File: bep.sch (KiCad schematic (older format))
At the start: 28 parts

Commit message: first version of schematic finished
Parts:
- removed D?: D, symbol Device:D
- removed JP?: Jumper, symbol Device:Jumper
- added C1: 100n, Capacitor_SMD:C_1206_3216Metric_Pad1.42x1.75mm_HandSolder, symbol Device:C
- added C?: 10u, symbol Device:CP
- added D4: D, symbol Device:D
- added D? (x4): LED, symbol Device:LED
- added J2: Conn_01x24, symbol Connector_Generic:Conn_01x24
- added Q1, Q2, Q3, Q4, Q5, Q6: SMBTA42, Package_TO_SOT_SMD:SOT-23, symbol Device:Q_NPN_BEC
- added R1, R2, R3: 100k, symbol Device:R
- added R10, R20, R4, R6, R7, R8, R9: 10k, symbol Device:R
- added R11, R12: 47 2W, symbol Device:R
- added R?: 100, symbol Device:R
- added R? (x4): 350, symbol Device:R
- added U1: HCF4028B, Package_SO:SOIC-16_3.9x9.9mm_P1.27mm, symbol 4xxx:4028
- added U2: LM1117-5.0, symbol Regulator_Linear:LM1117-5.0
- R16: renamed from R?; value 10k -> 100k
- gave numbers to parts that had none: 25
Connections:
- net labels added: 12V_IGN, GEAR1, GEAR2, GEAR3, GEAR4, GEAR5, GEAR_NEUTRAL
- net labels removed: 12V
- wire segments 96 -> 184
- no-connect marks 1 -> 5
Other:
- note added: "Decode gear signals"
- note added: "Provide excitation current for alternator"
- note added: "RMP signal"
- note removed: "INSERT 5V LDO here"
- note removed: "K100 Lunchbox Adapter"
- moved on the sheet: C2, D2, D3, J1, Q7, R13, R14, R15, R16, R17, R18, R19

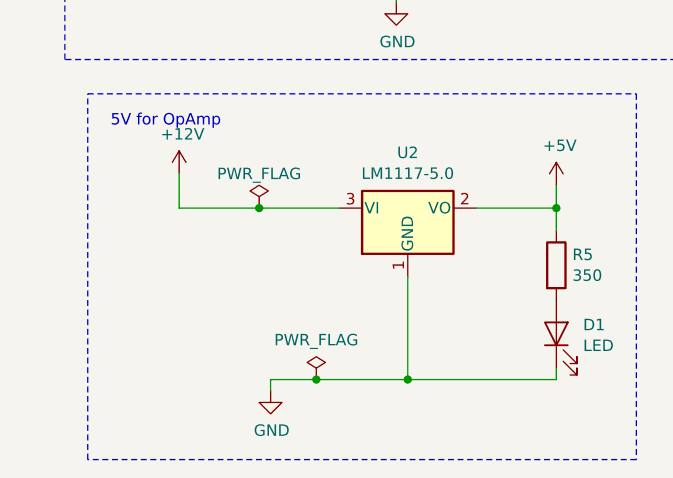
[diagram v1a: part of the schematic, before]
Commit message: add TSV diode to library
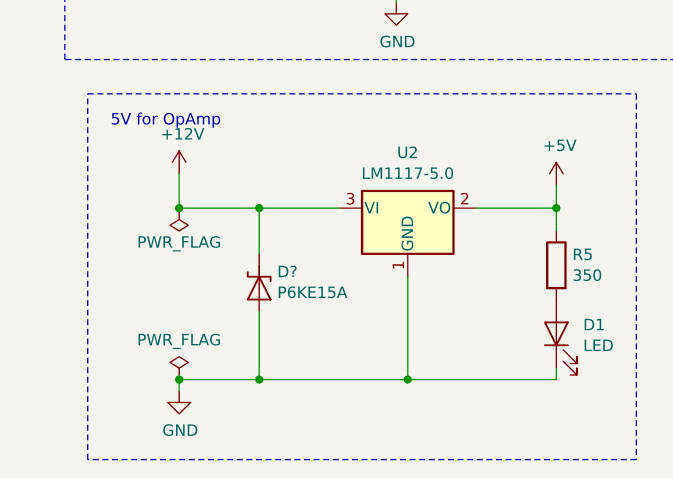
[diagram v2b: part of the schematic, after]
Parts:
- added D?: P6KE15A, Diode_THT:D_DO-15_P12.70mm_Horizontal, symbol bep:D_TVS_uni
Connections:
- wire segments 184 -> 186
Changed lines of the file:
@@
 $EndComp
 Wire Wire Line
-	1450 7350 1450 7300
-Wire Wire Line
-	1450 7300 1650 7300
-Connection ~ 1650 7300
+	1050 7350 1050 7300
+Connection ~ 1050 7300
 $Comp
 L power:PWR_FLAG #FLG0102
 U 1 1 5CCB4D9A
-P 1650 7300
-F 0 "#FLG0102" H 1650 7375 50  0001 C CNN
-F 1 "PWR_FLAG" H 1650 7473 50  0000 C CNN
-F 2 "" H 1650 7300 50  0001 C CNN
-F 3 "~" H 1650 7300 50  0001 C CNN
-	1    1650 7300
-	1    0    0    -1
-$EndComp
-Wire Wire Line
-	1400 6550 1750 6550
+P 1050 7300
+F 0 "#FLG0102" H 1050 7375 50  0001 C CNN
+F 1 "PWR_FLAG" H 1050 7473 50  0000 C CNN
+F 2 "" H 1050 7300 50  0001 C CNN
+F 3 "~" H 1050 7300 50  0001 C CNN
+	1    1050 7300
+	1    0    0    -1
+$EndComp
 Wire Wire Line
 	1050 6550 1400 6550
-Connection ~ 1400 6550
+Connection ~ 1050 6550
 $Comp
 L power:PWR_FLAG #FLG0101
 U 1 1 5CCB4539
-P 1400 6550
-F 0 "#FLG0101" H 1400 6625 50  0001 C CNN
-F 1 "PWR_FLAG" H 1400 6700 50  0000 C CNN
-F 2 "" H 1400 6550 50  0001 C CNN
-F 3 "~" H 1400 6550 50  0001 C CNN
-	1    1400 6550
-	1    0    0    -1
+P 1050 6550
+F 0 "#FLG0101" H 1050 6625 50  0001 C CNN
+F 1 "PWR_FLAG" H 1050 6700 50  0000 C CNN
+F 2 "" H 1050 6550 50  0001 C CNN
+F 3 "~" H 1050 6550 50  0001 C CNN
+	1    1050 6550
+	1    0    0    1
 $EndComp
 $Comp
@@
 L power:GND #PWR0101
 U 1 1 5CCB1309
-P 1450 7350
-F 0 "#PWR0101" H 1450 7100 50  0001 C CNN
-F 1 "GND" H 1455 7177 50  0000 C CNN
-F 2 "" H 1450 7350 50  0001 C CNN
-F 3 "" H 1450 7350 50  0001 C CNN
-	1    1450 7350
-	1    0    0    -1
-$EndComp
-Wire Wire Line
-	1650 7300 2050 7300
+P 1050 7350
+F 0 "#PWR0101" H 1050 7100 50  0001 C CNN
+F 1 "GND" H 1055 7177 50  0000 C CNN
+F 2 "" H 1050 7350 50  0001 C CNN
+F 3 "" H 1050 7350 50  0001 C CNN
+	1    1050 7350
+	1    0    0    -1
+$EndComp
+Wire Wire Line
+	1050 7300 1400 7300
 Wire Wire Line
 	2050 6850 2050 7300
@@
 Wire Notes Line
 	3500 6000 3500 7650
+$Comp
+L bep:D_TVS_uni D?
+U 1 1 5D24CD62
+P 1400 6850
+F 0 "D?" V 1379 6929 50  0000 L CNN
+F 1 "P6KE15A" V 1470 6929 50  0000 L CNN
+F 2 "Diode_THT:D_DO-15_P12.70mm_Horizontal" H 1400 6850 50  0001 C CNN
+F 3 "~" H 1400 6850 50  0001 C CNN
+	1    1400 6850
+	0    1    1    0
+$EndComp
+Wire Wire Line
+	1400 6750 1400 6550
+Connection ~ 1400 6550
+Wire Wire Line
+	1400 6550 1750 6550
+Wire Wire Line
+	1400 7000 1400 7300
+Connection ~ 1400 7300
+Wire Wire Line
+	1400 7300 2050 7300
 $EndSCHEMATC

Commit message: finished logic of schematic
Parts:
- removed C?: 10u, symbol Device:CP
- removed R?: 100, symbol Device:R
- removed U3: LTC2054, Package_TO_SOT_SMD:TSOT-23-5_HandSoldering, symbol bep:LTC2054
- added C? (x2): 10u, symbol Device:CP
- added C?: 220n, symbol Device:C
- added C?: 56n, symbol Device:C
- added C? (x2): 100n, symbol Device:C
- added D? (x2): D, symbol Device:D
- added JP?: Jumper_3_Bridged12, symbol Jumper:Jumper_3_Bridged12
- added Q? (x2): SMBTA42, Package_TO_SOT_SMD:SOT-23, symbol Device:Q_NPN_BEC
- added R?: 4.7k, symbol Device:R
- added R? (x2): 2.2k, symbol Device:R
- added R? (x5): 10k, symbol Device:R
- added R?: 1k, symbol Device:R
- added U? (x3): LM2904, symbol Amplifier_Operational:LM2904
- gave numbers to parts that had none: 9
- renumbered D9 to D10, D2 to D11, D3 to D12, D4 to D13, D10 to D14, D1 to D2, D6 to D7, D7 to D8, D8 to D9, JP2 to JP1, JP3 to JP2, JP4 to JP3, JP5 to JP4, R8 to R11, R9 to R13, R10 to R14, R11 to R15, R12 to R16, R13 to R17, R14 to R18, R15 to R19, R16 to R21, R17 to R22, R18 to R23, R19 to R24, R20 to R25
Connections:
- wire segments 186 -> 243
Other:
- note added: "Jumper position:\n1-2: 12V rect signal, pulse to GND\n2-3: filtered ignition coil signal"
- note added: "RPM Signal conditioning"
- note removed: "RMP signal"
- moved on the sheet: C2, D1, D11, D12, D13, D14, J1, J2, Q7, Q8, Q9, R15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

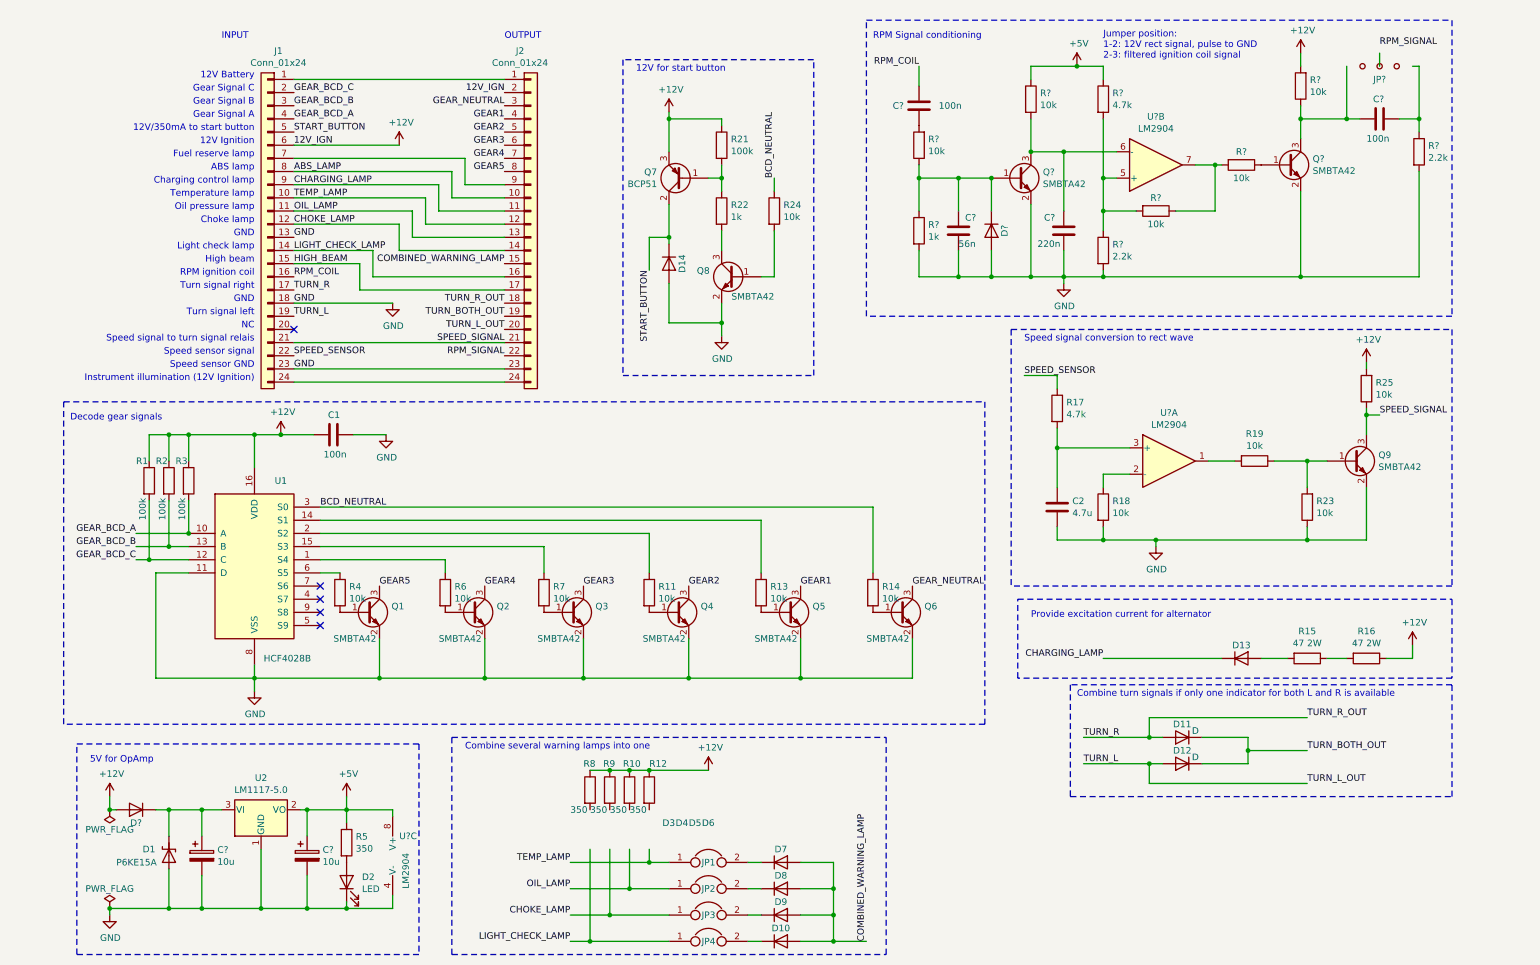
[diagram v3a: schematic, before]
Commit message: finalized schematic
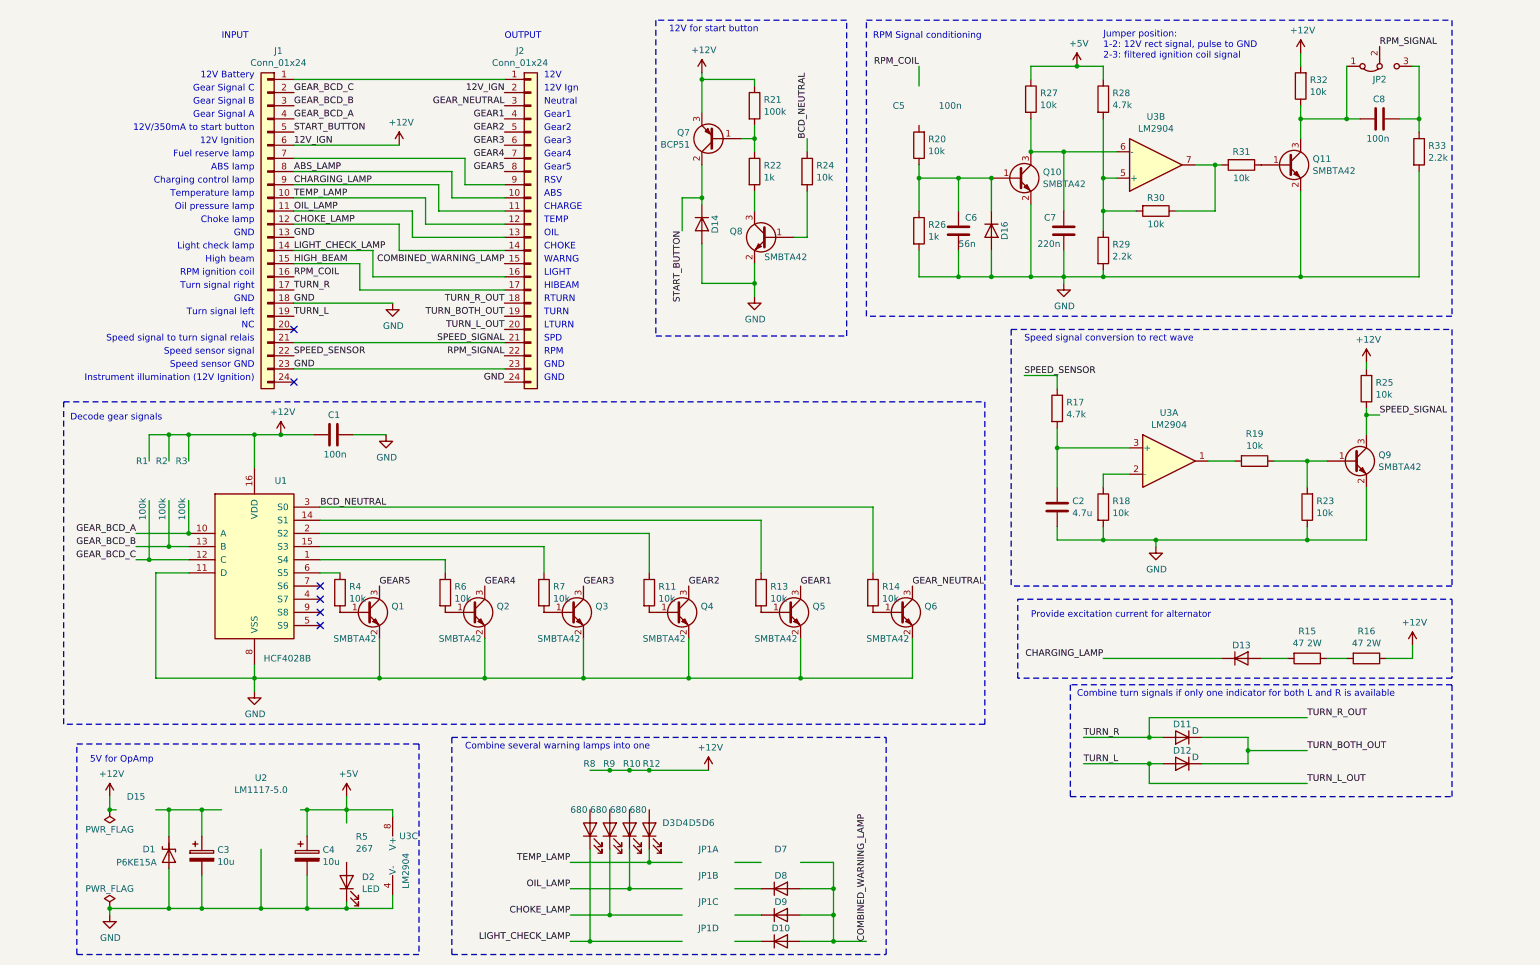
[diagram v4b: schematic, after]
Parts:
- removed JP1, JP2, JP3, JP4: Jumper, symbol Device:Jumper
- added JP1: Jumper_4x2, Connector_PinHeader_2.54mm:PinHeader_2x04_P2.54mm_Vertical, symbol bep:Jumper_4x2
- C2: footprint (none) -> Capacitor_SMD:C_1206_3216Metric_Pad1.42x1.75mm_HandSolder
- C3, C4: renamed from C?; footprint (none) -> Capacitor_SMD:CP_Elec_4x5.8
- C5: renamed from C?; footprint (none) -> Capacitor_THT:C_Rect_L18.0mm_W8.0mm_P15.00mm_FKS3_FKP3
- C6: renamed from C?; footprint (none) -> Capacitor_SMD:C_0603_1608Metric_Pad1.05x0.95mm_HandSolder
- C7, C8: renamed from C?; footprint (none) -> Capacitor_SMD:C_1206_3216Metric_Pad1.42x1.75mm_HandSolder
- D10, D11, D12, D13, D14, D7, D8, D9: footprint (none) -> Diode_SMD:D_SMA_Handsoldering
- D15, D16: renamed from D?; footprint (none) -> Diode_SMD:D_SMA_Handsoldering
- D2, D3, D4, D5, D6: footprint (none) -> LED_SMD:LED_1206_3216Metric_Pad1.42x1.75mm_HandSolder
- R1, R2, R21, R3: footprint (none) -> Resistor_SMD:R_1206_3216Metric_Pad1.42x1.75mm_HandSolder
- R10, R12, R8, R9: value 350 -> 680; footprint (none) -> Resistor_SMD:R_0805_2012Metric_Pad1.15x1.40mm_HandSolder
- R11, R13, R14, R17, R18, R19, R22, R23, R24, R25, R4, R6, R7: footprint (none) -> Resistor_SMD:R_0805_2012Metric_Pad1.15x1.40mm_HandSolder
- R15, R16: footprint (none) -> Resistor_THT:R_Axial_DIN0614_L14.3mm_D5.7mm_P25.40mm_Horizontal
- R20, R26, R27, R28, R29, R30, R31, R32, R33: renamed from R?; footprint (none) -> Resistor_SMD:R_0805_2012Metric_Pad1.15x1.40mm_HandSolder
- R5: value 350 -> 267; footprint (none) -> Resistor_SMD:R_1206_3216Metric_Pad1.42x1.75mm_HandSolder
- U2: footprint (none) -> Package_TO_SOT_SMD:SOT-223-3_TabPin2
- U3: renamed from U?; footprint (none) -> Package_SO:SO-8_3.9x4.9mm_P1.27mm
- gave numbers to parts that had none: 3
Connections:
- wire segments 243 -> 241
- no-connect marks 5 -> 6
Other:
- note added: "12V"
- note added: "12V Ign"
- note added: "ABS"
- note added: "CHARGE"
- note added: "CHOKE"
- note added: "Gear1"
- note added: "Gear2"
- note added: "Gear3"
- note added: "Gear4"
- note added: "Gear5"
- note added: "HIBEAM"
- note added: "LIGHT"
- note added: "LTURN"
- note added: "Neutral"
- note added: "OIL"
- note added: "RPM"
- note added: "RSV"
- note added: "RTURN"
- note added: "SPD"
- note added: "TEMP"
- note added: "TURN"
- note added: "WARNG"
- moved on the sheet: D14, Q7, Q8, R21, R22, R24

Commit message: output signals grouped to several connectors
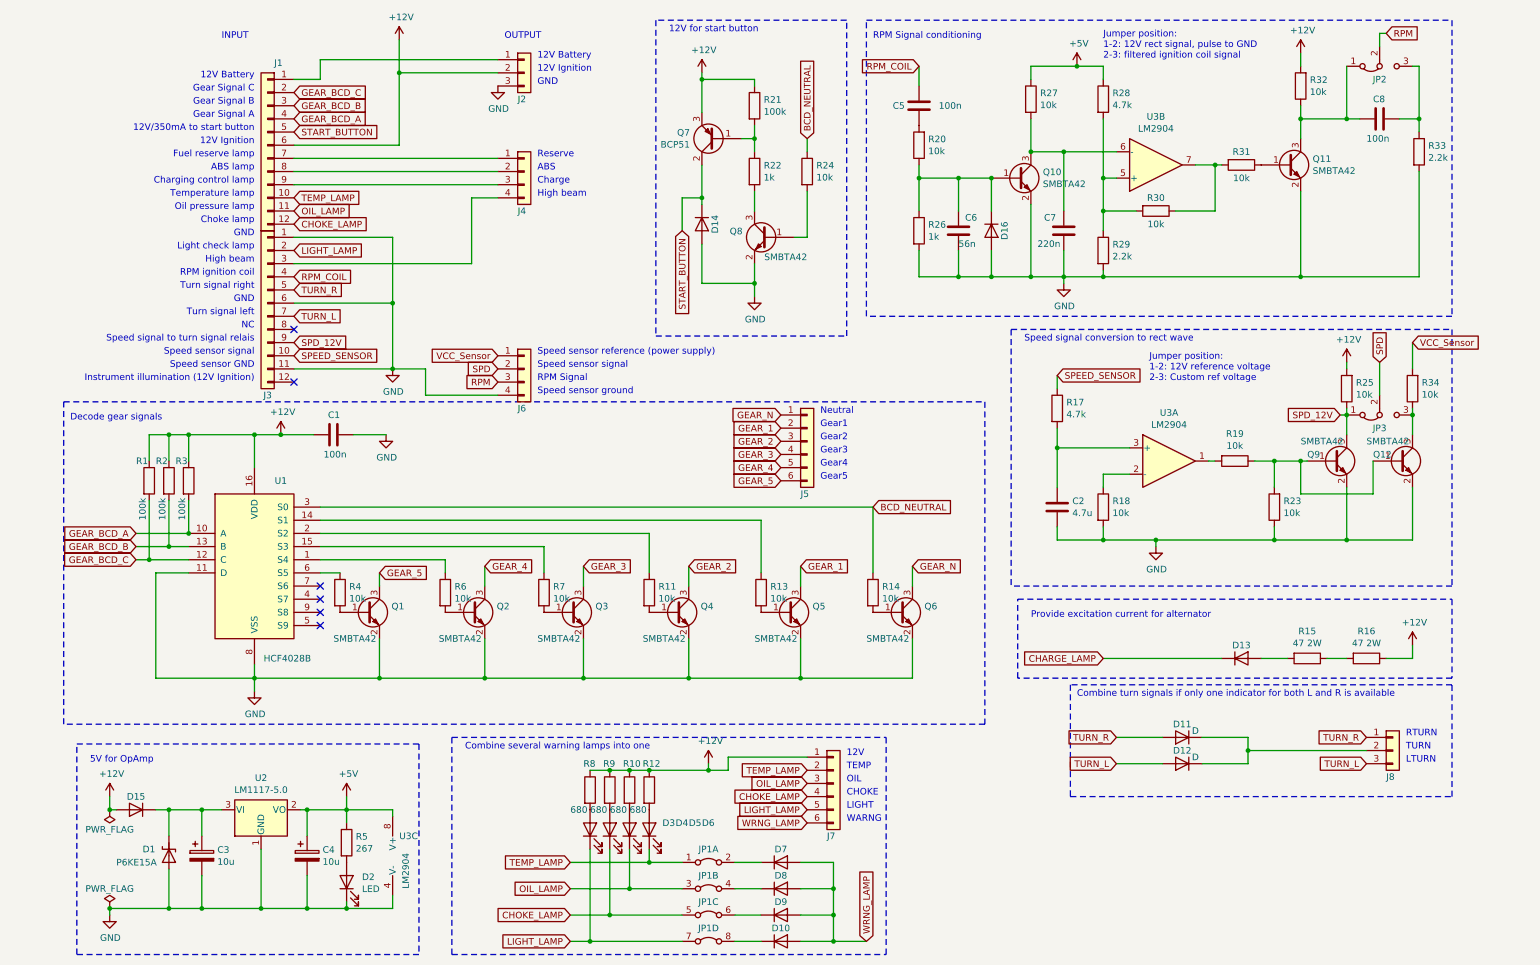
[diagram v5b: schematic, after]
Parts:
- removed J1, J2: Conn_01x24, symbol Connector_Generic:Conn_01x24
- added J1, J3: Conn_01x12, Connector_PinHeader_2.54mm:PinHeader_1x12_P2.54mm_Vertical, symbol Connector_Generic:Conn_01x12
- added J2, J8: Conn_01x03, Connector_PinHeader_2.54mm:PinHeader_1x03_P2.54mm_Vertical, symbol Connector_Generic:Conn_01x03
- added J4, J6: Conn_01x03, Connector_PinHeader_2.54mm:PinHeader_1x04_P2.54mm_Vertical, symbol Connector_Generic:Conn_01x04
- added J5, J7: Conn_01x06, Connector_PinHeader_2.54mm:PinHeader_1x06_P2.54mm_Vertical, symbol Connector_Generic:Conn_01x06
- added JP3: Jumper_3_Bridged12, Connector_PinHeader_2.54mm:PinHeader_1x03_P2.54mm_Vertical, symbol Jumper:Jumper_3_Bridged12
- added Q12: SMBTA42, Package_TO_SOT_SMD:SOT-23, symbol Device:Q_NPN_BEC
- added R34: 10k, Resistor_SMD:R_0805_2012Metric_Pad1.15x1.40mm_HandSolder, symbol Device:R
- D10, D11, D12, D13, D14, D15, D16, D7, D8, D9: footprint Diode_SMD:D_SMA_Handsoldering -> Diode_SMD:D_0603_1608Metric_Pad1.05x0.95mm_HandSolder
- JP2: footprint (none) -> Connector_PinHeader_2.54mm:PinHeader_1x03_P2.54mm_Vertical
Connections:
- net labels added: CHARGE_LAMP, GEAR_1, GEAR_2, GEAR_3, GEAR_4, GEAR_5, GEAR_N, LIGHT_LAMP, RPM, SPD, SPD_12V, VCC_Sensor, WRNG_LAMP
- net labels removed: 12V_IGN, ABS_LAMP, CHARGING_LAMP, COMBINED_WARNING_LAMP, GEAR1, GEAR2, GEAR3, GEAR4, GEAR5, GEAR_NEUTRAL, HIGH_BEAM, LIGHT_CHECK_LAMP, RPM_SIGNAL, SPEED_SIGNAL, TURN_BOTH_OUT, TURN_L_OUT, TURN_R_OUT
- wire segments 241 -> 248
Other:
- note added: "Charge"
- note added: "Jumper position:\n1-2: 12V reference voltage\n2-3: Custom ref voltage"
- note added: "RPM Signal"
- note added: "Reserve"
- note added: "Speed sensor ground"
- note added: "Speed sensor reference (power supply)"
- note removed: "12V Ign"
- note removed: "CHARGE"
- note removed: "HIBEAM"
- note removed: "RPM"
- note removed: "RSV"
- note removed: "SPD"
- moved on the sheet: Q9, R19, R23, R25

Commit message: begin pcb
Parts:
- renumbered C3 to C1, C4 to C2, C1 to C3, C5 to C4, C6 to C5, C2 to C6, D15 to D1, D8 to D10, D9 to D11, D10 to D12, D16 to D13, D11 to D14, D12 to D15, D13 to D16, D1 to D2, D2 to D3, D3 to D4, D4 to D5, D5 to D6, D6 to D7, D14 to D8, D7 to D9, J3 to J2, J2 to J3, J6 to J5, J5 to J6, Q11 to Q10, Q9 to Q11, Q7 to Q5, Q8 to Q6, Q5 to Q7, Q6 to Q8, Q10 to Q9, R21 to R13, R22 to R14, R13 to R15, R24 to R16, R14 to R17, R20 to R18, R26 to R19, R27 to R20, R17 to R21, R28 to R22, R29 to R23, R18 to R24, R30 to R25, R19 to R26, R31 to R27, R23 to R28, R32 to R29, R15 to R30, R25 to R31, R16 to R32, R34 to R33, R33 to R34
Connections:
- net CHARGE_LAMP: now also J1.9 (Pin_9), J4.3 (Pin_3)
